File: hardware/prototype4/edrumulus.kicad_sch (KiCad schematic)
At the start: 67 parts, among them J1 Trigger Connector, J2 Raspberry Pi GPIO pins, U1 ESP32-DEVKIT-V1

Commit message: diodes must have larger size on PCB
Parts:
- D1, D10, D11, D12, D13, D14, D15, D16, D17, D18, D19, D2, D20, D21, D22, D23, D24, D25, D26, D3, D4, D5, D6, D7, D8, D9: footprint Diode_SMD:D_0805_2012Metric_Pad1.15x1.40mm_HandSolder -> Diode_SMD:D_MiniMELF

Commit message: some more component reordering for prototype 4
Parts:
- R1, R10, R11, R12, R13, R14, R15, R16, R17, R18, R19, R2, R20, R21, R22, R23, R24, R25, R26, R27, R28, R29, R3, R30, R31, R32, R33, R34, R35, R36, R37, R38, R4, R5, R6, R7, R8, R9: footprint Resistor_SMD:R_0805_2012Metric_Pad1.15x1.40mm_HandSolder -> Resistor_SMD:R_1206_3216Metric_Pad1.30x1.75mm_HandSolder

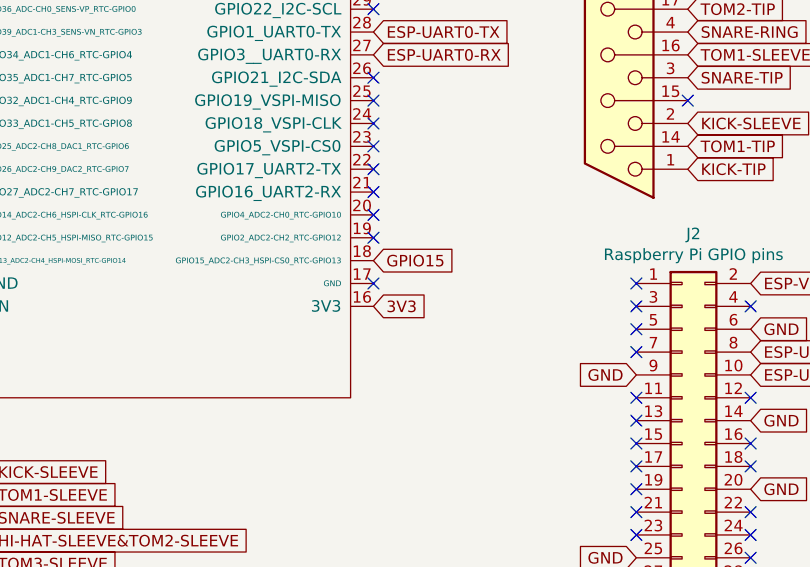
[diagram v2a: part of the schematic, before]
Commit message: added an additional GND to the ESP32 board
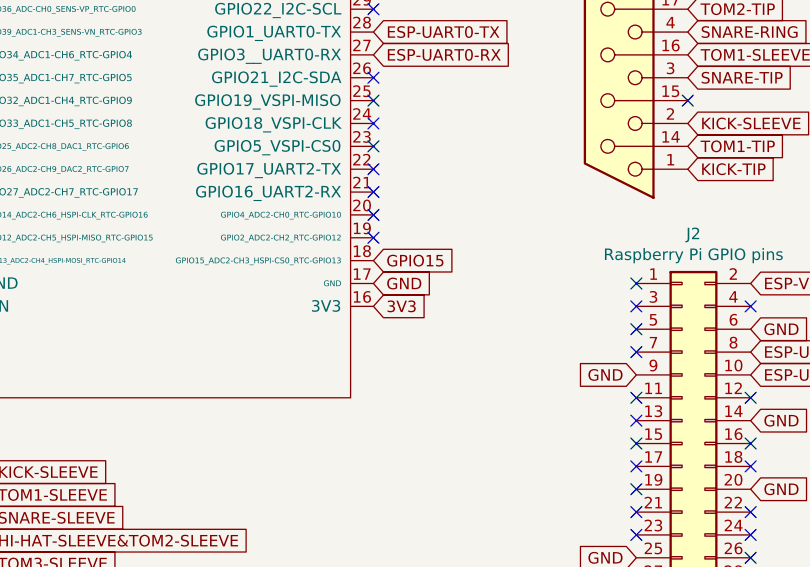
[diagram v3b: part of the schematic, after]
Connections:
- net CRASH1-SLEEVE: now also U1.17 (GND)
- no-connect marks 46 -> 45
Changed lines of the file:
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@@
   (no_connect (at 252.095 131.445))
   (no_connect (at 252.095 146.685))
-  (no_connect (at 210.185 100.965))
   (no_connect (at 210.185 83.185))
   (no_connect (at 252.095 113.665))
@@
       (effects (font (size 1.27 1.27)) hide)
     )
+  )
+  (global_label "GND" (shape input) (at 210.185 100.965 0) (fields_autoplaced)
+    (effects (font (size 1.27 1.27)) (justify left))
+    (property "Referenzen zwischen Schaltplänen" "${INTERSHEET_REFS}" (id 0) (at 373.38 201.93 0)
+      (effects (font (size 1.27 1.27)) hide)
+    )
